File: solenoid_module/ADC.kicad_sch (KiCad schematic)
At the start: 2 parts, among them U2 ADS1115IDGS

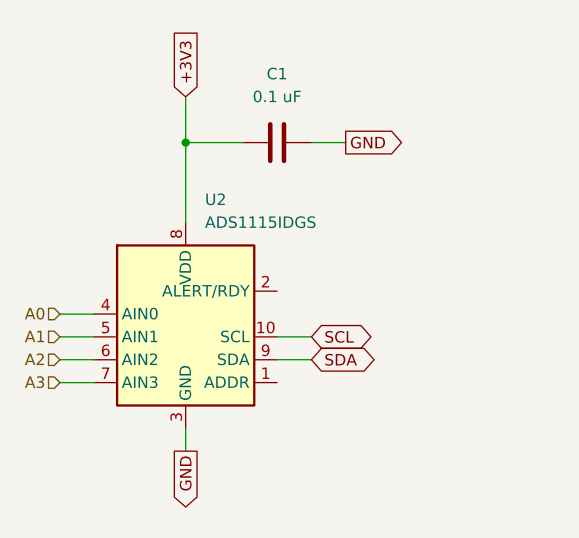
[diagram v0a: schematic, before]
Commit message: Solenoid module wiring
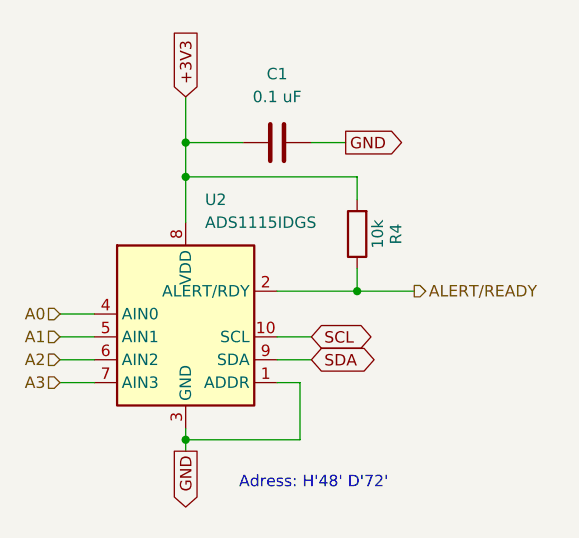
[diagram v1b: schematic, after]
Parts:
- added R4: 10k, Resistor_SMD:R_0603_1608Metric_Pad0.98x0.95mm_HandSolder, symbol Device:R
- C1: footprint (none) -> Capacitor_SMD:C_0603_1608Metric_Pad1.08x0.95mm_HandSolder
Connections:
- net +3V3: now also R4.2
- net GND: now also U2.1 (ADDR)
- net ALERT/READY: now reaches U2.2 (ALERT/RDY)
- net ALERT/READY: now also R4.1
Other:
- note added: "Adress: H'48' D'72'"
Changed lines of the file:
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@@
 	(generator_version "9.0")
 	(paper "A4")
+	(text "Adress: H'48' D'72'"
+		(exclude_from_sim no)
+		(at 80.264 67.056 0)
+		(effects
+			(font
+				(size 1.27 1.27)
+			)
+		)
+	)
 	(junction
 		(at 66.04 29.21)
@@
 		(color 0 0 0 0)
 	)
+	(junction
+		(at 85.09 45.72)
+		(diameter 0)
+		(color 0 0 0 0)
+	)
+	(junction
+		(at 66.04 62.23)
+		(diameter 0)
+		(color 0 0 0 0)
+	)
+	(junction
+		(at 66.04 33.02)
+		(diameter 0)
+		(color 0 0 0 0)
+	)
 	(wire
 		(pts
@@
 	(wire
 		(pts
+			(xy 85.09 43.18) (xy 85.09 45.72)
+		)
+		(stroke
+			(width 0)
+			(type default)
+		)
+	)
+	(wire
+		(pts
 			(xy 76.2 50.8) (xy 80.01 50.8)
 		)
@@
 	(wire
 		(pts
+			(xy 85.09 45.72) (xy 91.44 45.72)
+		)
+		(stroke
+			(width 0)
+			(type default)
+		)
+	)
+	(wire
+		(pts
 			(xy 80.01 29.21) (xy 83.82 29.21)
 		)
@@
 	(wire
 		(pts
+			(xy 76.2 45.72) (xy 85.09 45.72)
+		)
+		(stroke
+			(width 0)
+			(type default)
+		)
+	)
+	(wire
+		(pts
 			(xy 52.07 50.8) (xy 55.88 50.8)
 		)
@@
 	(wire
 		(pts
+			(xy 78.74 55.88) (xy 78.74 62.23)
+		)
+		(stroke
+			(width 0)
+			(type default)
+		)
+	)
+	(wire
+		(pts
 			(xy 52.07 53.34) (xy 55.88 53.34)
 		)
@@
 	(wire
 		(pts
+			(xy 66.04 33.02) (xy 66.04 38.1)
+		)
+		(stroke
+			(width 0)
+			(type default)
+		)
+	)
+	(wire
+		(pts
+			(xy 66.04 62.23) (xy 66.04 63.5)
+		)
+		(stroke
+			(width 0)
+			(type default)
+		)
+	)
+	(wire
+		(pts
+			(xy 66.04 62.23) (xy 78.74 62.23)
+		)
+		(stroke
+			(width 0)
+			(type default)
+		)
+	)
+	(wire
+		(pts
+			(xy 76.2 55.88) (xy 78.74 55.88)
+		)
+		(stroke
+			(width 0)
+			(type default)
+		)
+	)
+	(wire
+		(pts
+			(xy 66.04 33.02) (xy 85.09 33.02)
+		)
+		(stroke
+			(width 0)
+			(type default)
+		)
+	)
+	(wire
+		(pts
+			(xy 85.09 35.56) (xy 85.09 33.02)
+		)
+		(stroke
+			(width 0)
+			(type default)
+		)
+	)
+	(wire
+		(pts
 			(xy 52.07 48.26) (xy 55.88 48.26)
 		)
@@
 	(wire
 		(pts
-			(xy 66.04 60.96) (xy 66.04 63.5)
+			(xy 66.04 60.96) (xy 66.04 62.23)
 		)
 		(stroke
@@
 	(wire
 		(pts
-			(xy 66.04 29.21) (xy 66.04 38.1)
+			(xy 66.04 29.21) (xy 66.04 33.02)
 		)
 		(stroke
@@
 			)
 			(justify right)
+		)
+	)
+	(hierarchical_label "ALERT{slash}READY"
+		(shape output)
+		(at 91.44 45.72 0)
+		(effects
+			(font
+				(size 1.27 1.27)
+			)
+			(justify left)
+		)
+	)
+	(symbol
+		(lib_id "Device:R")
+		(at 85.09 39.37 180)
+		(unit 1)
+		(exclude_from_sim no)
+		(in_bom yes)
+		(on_board yes)
+		(dnp no)
+		(property "Reference" "R4"
+			(at 89.408 39.37 90)
+			(effects
+				(font
+					(size 1.27 1.27)
+				)
+			)
+		)
+		(property "Value" "10k"
+			(at 87.376 39.37 90)
+			(effects
+				(font
+					(size 1.27 1.27)
+				)
+			)
+		)
+		(property "Footprint" "Resistor_SMD:R_0603_1608Metric_Pad0.98x0.95mm_HandSolder"
+			(at 86.868 39.37 90)
+			(effects
+				(font
+					(size 1.27 1.27)
+				)
+				(hide yes)
+			)
+		)
+		(property "Datasheet" "~"
+			(at 85.09 39.37 0)
+			(effects
+				(font
+					(size 1.27 1.27)
+				)
+				(hide yes)
+			)
+		)
+		(property "Description" "Resistor"
+			(at 85.09 39.37 0)
+			(effects
+				(font
+					(size 1.27 1.27)
+				)
+				(hide yes)
+			)
+		)
+		(property "Manufacturer Part Number" "RC0603FR-0710KL"
+			(at 85.09 39.37 0)
+			(effects
+				(font
+					(size 1.27 1.27)
+				)
+				(hide yes)
+			)
+		)
+		(property "Mouser number" "603-RC0603FR-0710KL"
+			(at 85.09 39.37 0)
+			(effects
+				(font
+					(size 1.27 1.27)
+				)
+				(hide yes)
+			)
+		)
+		(property "Ullmanna Part Number" "BMCR0201"
+			(at 85.09 39.37 90)
+			(effects
+				(font
+					(size 1.27 1.27)
+				)
+				(hide yes)
+			)
+		)
+		(pin "2"
+		)
+		(pin "1"
+		)
+		(instances
+			(project "solenoid_module"
+				(path "/b7f24f9f-04e9-4f9d-9a73-f222f75554b4/357714fe-9dd7-44fd-a978-2dc509f551c4"
+					(reference "R4")
+					(unit 1)
+				)
+			)
 		)
 	)
@@
 			)
 		)
-		(property "Footprint" ""
+		(property "Footprint" "Capacitor_SMD:C_0603_1608Metric_Pad1.08x0.95mm_HandSolder"
 			(at 80.01 28.2448 0)
 			(effects

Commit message: PCB update
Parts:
- R4: Mouser Part Number (none) -> 603-RC0603FR-0710KL
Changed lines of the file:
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@@
+			)
+		)
+		(property "Mouser Part Number" "603-RC0603FR-0710KL "
+			(at 85.09 39.37 90)
+			(effects
+				(font
+					(size 1.27 1.27)
+				)
+				(hide yes)
 			)
 		)
